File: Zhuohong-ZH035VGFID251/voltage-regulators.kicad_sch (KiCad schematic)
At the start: 10 parts, among them U1 RS3236-1.8FY5, U3 AP3127B

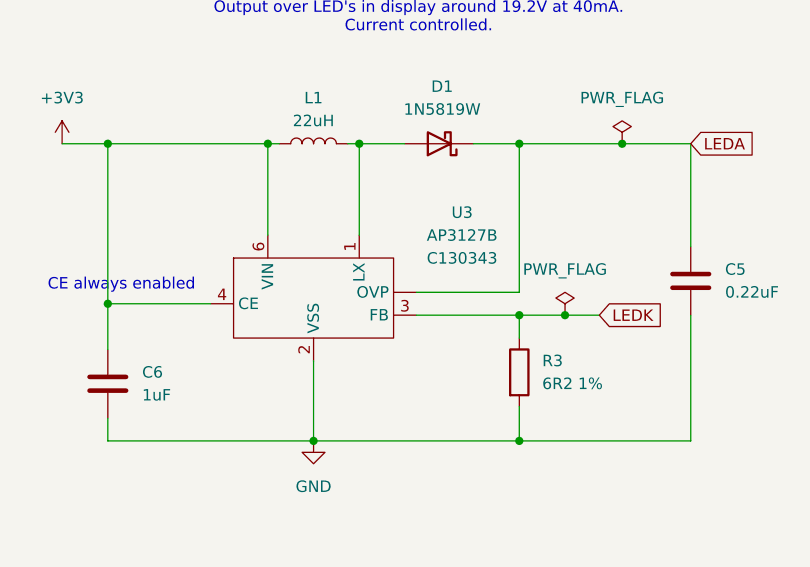
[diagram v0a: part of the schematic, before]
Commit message: Fix names, footprints, and silkscreen of the pcb's
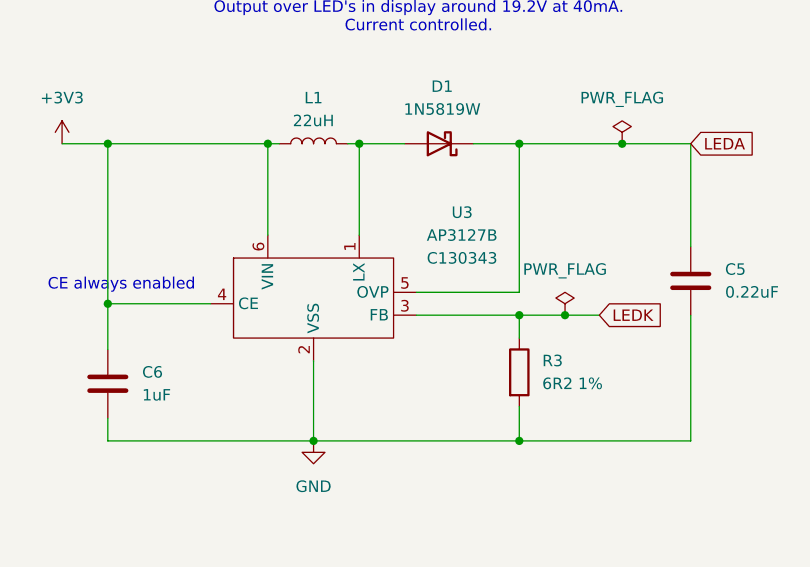
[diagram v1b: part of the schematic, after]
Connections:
- net LEDA: now also U3.5 (OVP); no longer U3. (OVP)
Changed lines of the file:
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@@
 		(pin "1"
 		)
-		(pin ""
+		(pin "5"
 		)
 		(pin "2"
